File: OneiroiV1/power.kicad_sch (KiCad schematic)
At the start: 57 parts, among them J1 Conn_02x04_Odd_Even, J13 TB002-500-02BE, J14 TB002-500-02BE, J15 TB002-500-02BE, J16 TB002-500-02BE, J4 Conn_01x02, J6 Conn_02x04_Odd_Even, U13 TPS2121RUXT, U14 TPS2121RUXT, U22 TPS63070RNMR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

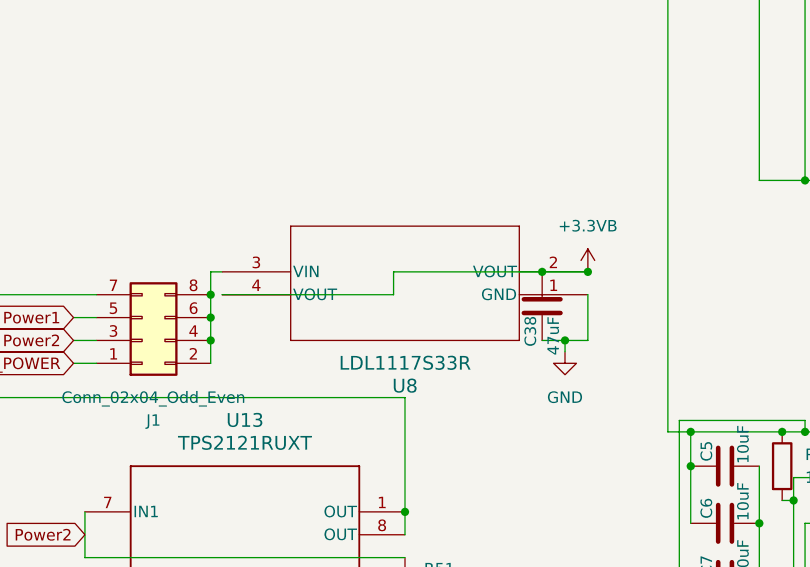
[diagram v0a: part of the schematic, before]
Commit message: Oneiroi Changes
All 3D models and footprints updated to common library, silkscreening must be re-done.
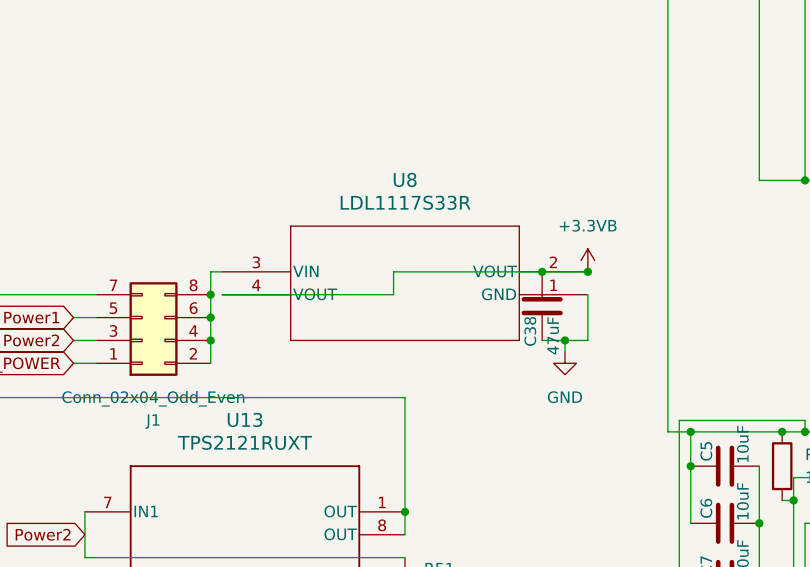
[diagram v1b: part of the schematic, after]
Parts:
- J13, J14, J15, J16: footprint screw terminal:CUI_TB002-500-02BE -> UNSW Rocketry Library:CUI_TB002-500-02BE; symbol screw terminal:TB002-500-02BE -> UNSW Rocketry Library:TB002-500-02BE
- L1, L2: footprint inductor:1277AS-H-1R0M=P2_MUR-M -> UNSW Rocketry Library:1277AS-H-1R0M=P2_MUR-M
- U13, U14: footprint TPS2121:RUX0012A -> UNSW Rocketry Library:RUX0012A; symbol Piority Voltage Switcher:TPS2121RUXT -> UNSW Rocketry Library:TPS2121RUXT
- U22, U23: footprint TPS63070:RNM0015A -> UNSW Rocketry Library:RNM0015A; symbol TPS63070:TPS63070RNMR -> UNSW Rocketry Library:TPS63070RNMR
- U8: footprint LDO:SOT223_STM -> UNSW Rocketry Library:SOT223_STM; symbol 3V3 LDO:LDL1117S33R -> UNSW Rocketry Library:LDL1117S33R
- U9: footprint Ideal Diode:SOT-5X3_DRL_TEX -> UNSW Rocketry Library:SOT-5X3_DRL_TEX; symbol Ideal Diode:LM66200DRLR -> UNSW Rocketry Library:LM66200DRLR
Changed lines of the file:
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@@
 	)
 	(symbol
-		(lib_id "TPS63070:TPS63070RNMR")
+		(lib_id "UNSW Rocketry Library:TPS63070RNMR")
 		(at 233.68 212.09 0)
 		(unit 1)
@@
 			)
 		)
-		(property "Footprint" "TPS63070:RNM0015A"
+		(property "Footprint" "UNSW Rocketry Library:RNM0015A"
 			(at 233.68 212.09 0)
 			(hide yes)
@@
 	)
 	(symbol
-		(lib_id "3V3 LDO:LDL1117S33R")
+		(lib_id "UNSW Rocketry Library:LDL1117S33R")
 		(at 187.96 184.15 180)
 		(unit 1)
@@
 		(fields_autoplaced yes)
 		(property "Reference" "U8"
-			(at 167.64 194.31 0)
+			(at 167.64 171.45 0)
 			(show_name no)
 			(do_not_autoplace no)
@@
 		)
 		(property "Value" "LDL1117S33R"
-			(at 167.64 191.77 0)
+			(at 167.64 173.99 0)
 			(show_name no)
 			(do_not_autoplace no)
@@
 			)
 		)
-		(property "Footprint" "LDO:SOT223_STM"
+		(property "Footprint" "UNSW Rocketry Library:SOT223_STM"
 			(at 187.96 184.15 0)
 			(hide yes)
@@
 	)
 	(symbol
-		(lib_id "TPS63070:TPS63070RNMR")
+		(lib_id "UNSW Rocketry Library:TPS63070RNMR")
 		(at 233.68 139.7 0)
 		(unit 1)
@@
 			)
 		)
-		(property "Footprint" "TPS63070:RNM0015A"
+		(property "Footprint" "UNSW Rocketry Library:RNM0015A"
 			(at 233.68 139.7 0)
 			(hide yes)
@@
 	)
 	(symbol
-		(lib_id "screw terminal:TB002-500-02BE")
+		(lib_id "UNSW Rocketry Library:TB002-500-02BE")
 		(at 370.84 167.64 0)
 		(unit 1)
@@
 			)
 		)
-		(property "Footprint" "screw terminal:CUI_TB002-500-02BE"
+		(property "Footprint" "UNSW Rocketry Library:CUI_TB002-500-02BE"
 			(at 370.84 167.64 0)
 			(hide yes)
@@
 	)
 	(symbol
-		(lib_id "Ideal Diode:LM66200DRLR")
+		(lib_id "UNSW Rocketry Library:LM66200DRLR")
 		(at 337.82 111.76 0)
 		(unit 1)
@@
 			)
 		)
-		(property "Footprint" "Ideal Diode:SOT-5X3_DRL_TEX"
+		(property "Footprint" "UNSW Rocketry Library:SOT-5X3_DRL_TEX"
 			(at 337.82 111.76 0)
 			(hide yes)
@@
 			)
 		)
-		(property "Footprint" "inductor:1277AS-H-1R0M=P2_MUR-M"
+		(property "Footprint" "UNSW Rocketry Library:1277AS-H-1R0M=P2_MUR-M"
 			(at 233.68 107.95 0)
 			(hide yes)
@@
 	)
 	(symbol
-		(lib_id "Piority Voltage Switcher:TPS2121RUXT")
+		(lib_id "UNSW Rocketry Library:TPS2121RUXT")
 		(at 149.86 228.6 0)
 		(unit 1)
@@
 			)
 		)
-		(property "Footprint" "TPS2121:RUX0012A"
+		(property "Footprint" "UNSW Rocketry Library:RUX0012A"
 			(at 149.86 228.6 0)
 			(hide yes)
@@
 			)
 		)
-		(property "Footprint" "inductor:1277AS-H-1R0M=P2_MUR-M"
+		(property "Footprint" "UNSW Rocketry Library:1277AS-H-1R0M=P2_MUR-M"
 			(at 233.68 180.34 0)
 			(hide yes)
@@
 	)
 	(symbol
-		(lib_id "screw terminal:TB002-500-02BE")
+		(lib_id "UNSW Rocketry Library:TB002-500-02BE")
 		(at 295.91 218.44 180)
 		(unit 1)
@@
 			)
 		)
-		(property "Footprint" "screw terminal:CUI_TB002-500-02BE"
+		(property "Footprint" "UNSW Rocketry Library:CUI_TB002-500-02BE"
 			(at 295.91 218.44 0)
 			(hide yes)
@@
 	)
 	(symbol
-		(lib_id "Piority Voltage Switcher:TPS2121RUXT")
+		(lib_id "UNSW Rocketry Library:TPS2121RUXT")
 		(at 142.24 102.87 0)
 		(unit 1)
@@
 			)
 		)
-		(property "Footprint" "TPS2121:RUX0012A"
+		(property "Footprint" "UNSW Rocketry Library:RUX0012A"
 			(at 142.24 102.87 0)
 			(hide yes)
@@
 	)
 	(symbol
-		(lib_id "screw terminal:TB002-500-02BE")
+		(lib_id "UNSW Rocketry Library:TB002-500-02BE")
 		(at 320.04 165.1 0)
 		(mirror x)
@@
 			)
 		)
-		(property "Footprint" "screw terminal:CUI_TB002-500-02BE"
+		(property "Footprint" "UNSW Rocketry Library:CUI_TB002-500-02BE"
 			(at 320.04 165.1 0)
 			(hide yes)
@@
 	)
 	(symbol
-		(lib_id "screw terminal:TB002-500-02BE")
+		(lib_id "UNSW Rocketry Library:TB002-500-02BE")
 		(at 347.98 218.44 0)
 		(mirror y)
@@
 			)
 		)
-		(property "Footprint" "screw terminal:CUI_TB002-500-02BE"
+		(property "Footprint" "UNSW Rocketry Library:CUI_TB002-500-02BE"
 			(at 347.98 218.44 0)
 			(hide yes)
